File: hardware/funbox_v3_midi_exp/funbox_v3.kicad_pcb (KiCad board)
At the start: 2 copper layers, 59.7 x 67.5 mm, 70 parts, among them J6 MIDI IN JACK, J7 EXPRESSION, SW1 SW_SPDT, SW2 SW_SPDT, SW3 SW_SPDT, U1 TL074, U2 L7805, U3 TL072, U5 H11L1

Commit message: Updated to version 3.1, fix expression, adjusted pieces
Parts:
- J6: value MIDI IN JACK -> MIDI IN
- U3: value TL072 -> MCP6002
- moved R5 10.7 mm to (154.0, 129.9)
- moved R30 7.37 mm to (132.1, 66.4), turned to 0 degrees
- moved C30 6.62 mm to (133.4, 68.9), turned to -90 degrees
- moved R1 5.49 mm to (143.9, 129.9)
- moved C3 3.08 mm to (146.7, 126.8)
- moved C9 3.05 mm to (139.0, 126.9)
- moved R2 3.03 mm to (133.8, 129.9)
- moved S1 1.51 mm to (123.8, 117.0)
- moved J7 1.34 mm to (176.3, 71.2)
- moved J6 1.32 mm to (119.6, 71.2)
- moved 9v 0.83 mm to (144.2, 66.0)
- moved Gnd 0.80 mm to (148.2, 66.0)
- moved R19 0.73 mm to (162.9, 66.4)
- moved D2 0.67 mm to (136.2, 69.0)
- moved R31 0.59 mm to (138.9, 69.0)
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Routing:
- net Net-(U1A-+): track 27.0 -> 19.7 mm
- net DIP2: track 30.8 -> 25.1 mm
- net FOOT_SWITCH_2: track 74.9 -> 70.5 mm
- net Net-(D2-K): track 12.5 -> 8.27 mm
- net MIDI_IN_JACK_PIN4: track 9.64 -> 7.29 mm
- net MIDI_IN_JACK_PIN5: track 19.9 -> 17.7 mm
- net Net-(U1B-+): track 59.2 -> 61.2 mm
- net DIP1: track 23.9 -> 25.4 mm
- net EXPRESSION_REF: track 21.6 -> 20.3 mm
- net VCC: track 62.9 -> 64.1 mm
- net DIP4: track 41.2 -> 40.1 mm
- net DIP3: track 39.9 -> 38.8 mm
- net 3V3_A: track 153.9 -> 154.9 mm
- net EXPRESSION_IN_JACK: track 12.0 -> 11.0 mm
- net MIDI_IN: track 26.8 -> 27.6 mm
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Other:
- board text added: "FunBox v3.1 GuitarML"
- board text removed: "FunBox v3 GuitarML"

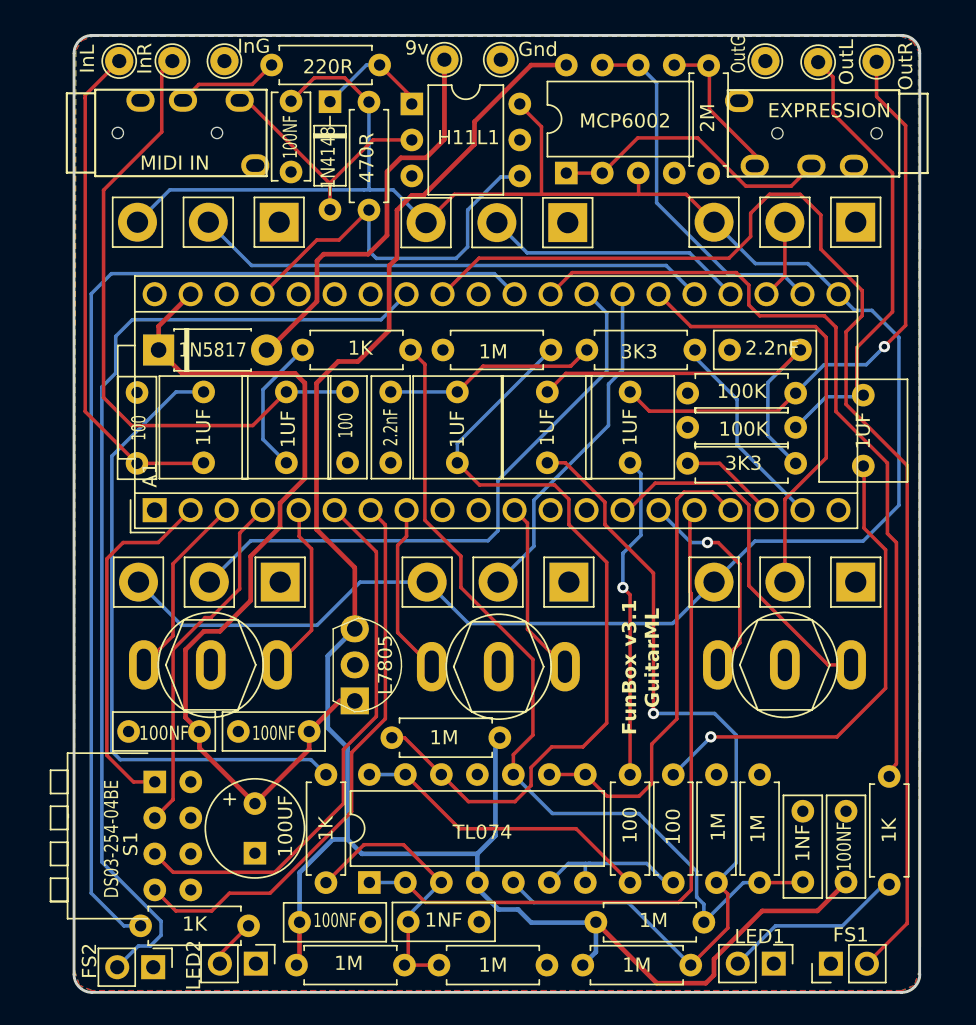
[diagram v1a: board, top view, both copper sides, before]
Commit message: Added pF label for clarity
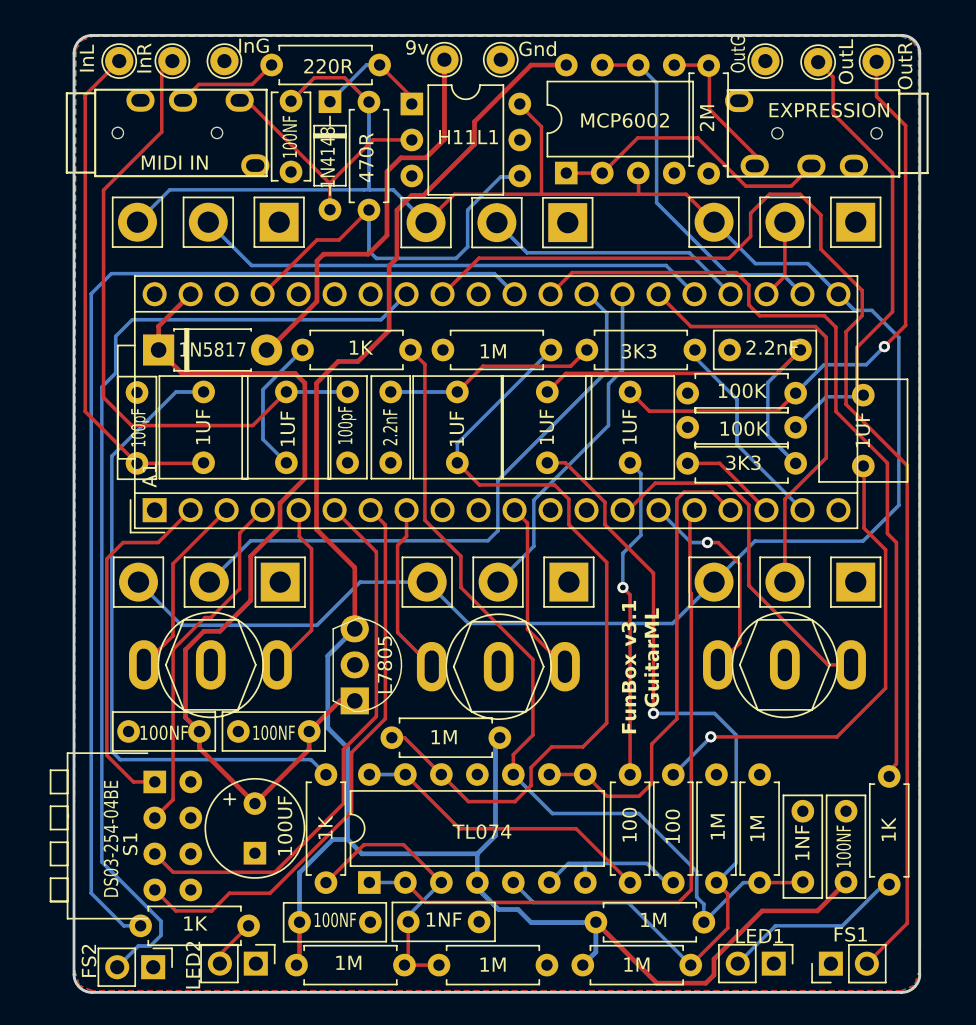
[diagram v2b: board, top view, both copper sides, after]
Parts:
- C11, C2: value 100 -> 100pF
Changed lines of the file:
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@@
         (effects (font (size 1 1) (thickness 0.15)))
     )
-    (fp_text value "100" (at 2.373 0.127 90) (layer "F.SilkS")
-        (effects (font (size 1 0.6952) (thickness 0.15)))
+    (fp_text value "100pF" (at 2.373 0.127 90) (layer "F.SilkS")
+        (effects (font (size 1 0.652) (thickness 0.15)))
     )
     (fp_text user "${REFERENCE}" (at 2.5 0 90) (layer "F.Fab")
@@
     )
     (fp_text value "100NF" (at 2.5 0.127 90) (layer "F.SilkS")
-        (effects (font (size 1 0.7968) (thickness 0.15)))
+        (effects (font (size 1 0.7) (thickness 0.15)))
     )
     (fp_text user "${REFERENCE}" (at 2.5 0 90) (layer "F.Fab")
@@
         (effects (font (size 1 1) (thickness 0.15)))
     )
-    (fp_text value "100" (at 2.5 0.127 90) (layer "F.SilkS")
-        (effects (font (size 1 0.6952) (thickness 0.15)))
+    (fp_text value "100pF" (at 2.5 0.127 90) (layer "F.SilkS")
+        (effects (font (size 1 0.652) (thickness 0.15)))
     )
     (fp_text user "${REFERENCE}" (at 2.5 0 90) (layer "F.Fab")

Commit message: Updated board to v3.2 to use MCP6024 op amp instead of TL074
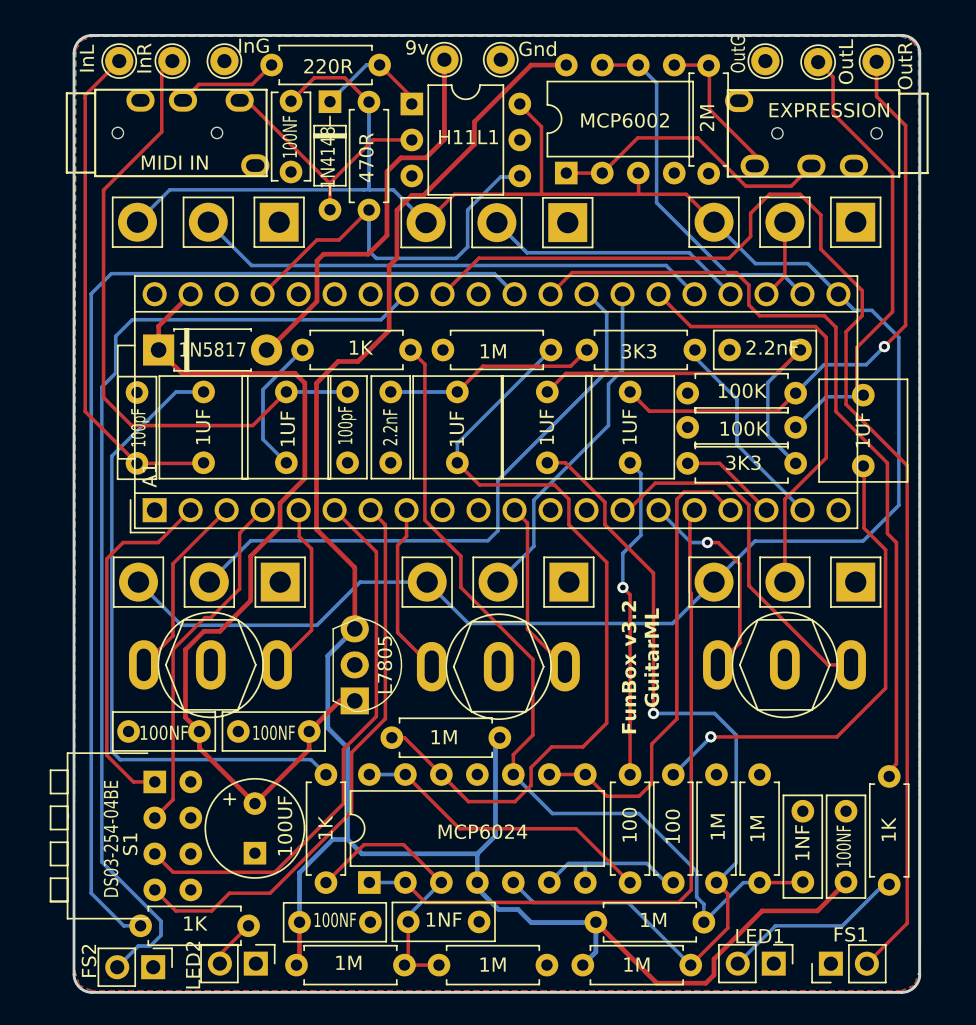
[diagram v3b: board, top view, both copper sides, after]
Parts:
- U1: value TL074 -> MCP6024
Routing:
- net GND: track 1.72 -> 0.00 mm
- net 5V: track 135.6 -> 134.9 mm
- net LED_1: track 57.7 -> 57.0 mm
- net unconnected-(A1-I2C1_SCL-Pad12): track 0.51 -> 0.00 mm
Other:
- board text added: "FunBox v3.2 GuitarML"
- board text removed: "FunBox v3.1 GuitarML"
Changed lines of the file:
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@@
       (plotinvisibletext false)
       (sketchpadsonfab false)
-      (subtractmaskfromsilk false)
+      (subtractmaskfromsilk true)
       (outputformat 1)
       (mirror false)
       (drillshape 0)
       (scaleselection 1)
-      (outputdirectory "GerberSeed/")
+      (outputdirectory "GerberSeed_PCBway_Funbox_v3p2/")
     )
   )
@@
         (effects (font (size 1 1) (thickness 0.15)))
     )
-    (fp_text value "TL074" (at 3.546 7.986 180) (layer "F.SilkS")
+    (fp_text value "MCP6024" (at 3.546 7.986 180) (layer "F.SilkS")
         (effects (font (size 1 1) (thickness 0.15)))
     )
@@
   (gr_line (start 118.11 130.556) (end 118.11 65.5574)
     (stroke (width 0.2) (type default)) (layer "Edge.Cuts"))
-  (gr_text "FunBox v3.1\n    GuitarML" (at 159.512 113.665 90) (layer "F.SilkS")
+  (gr_text "FunBox v3.2\n    GuitarML" (at 159.512 113.665 90) (layer "F.SilkS")
     (effects (font (size 1 1) (thickness 0.2) bold) (justify left bottom))
   )
@@
   (segment (start 139.7796 84.35) (end 122.225 84.35) (width 0.25) (layer "B.Cu") (net 5))
   (segment (start 121.05 88.119) (end 120.075 89.094) (width 0.25) (layer "B.Cu") (net 5))
-  (segment (start 121.478991 130.048) (end 121.158 130.048) (width 0.25) (layer "B.Cu") (net 5))
   (segment (start 123.5 128.55) (end 122.656 128.55) (width 0.25) (layer "B.Cu") (net 5))
   (segment (start 122.225 84.35) (end 121.05 85.525) (width 0.25) (layer "B.Cu") (net 5))
@@
   (segment (start 134 99.65) (end 134 97.8304) (width 0.25) (layer "F.Cu") (net 7))
   (segment (start 134.875 100.525) (end 134 99.65) (width 0.25) (layer "F.Cu") (net 7))
-  (segment (start 133.704004 97.79) (end 133.9596 97.79) (width 0.25) (layer "F.Cu") (net 7))
   (segment (start 132.4356 108.712) (end 134.875 106.2726) (width 0.25) (layer "F.Cu") (net 7))
   (segment (start 134 97.8304) (end 133.9596 97.79) (width 0.25) (layer "F.Cu") (net 7))
@@
   (segment (start 140.95 106.4314) (end 140.95 100.271301) (width 0.25) (layer "F.Cu") (net 9))
   (segment (start 141.5796 99.641701) (end 141.5796 97.79) (width 0.25) (layer "F.Cu") (net 9))
-  (segment (start 152.2476 97.79) (end 151.7396 97.79) (width 0.25) (layer "F.Cu") (net 10))
   (segment (start 161.671 103.666364) (end 161.671 124.587) (width 0.25) (layer "F.Cu") (net 14))
   (segment (start 161.5788 98.1108) (end 161.5788 103.574164) (width 0.25) (layer "F.Cu") (net 14))
@@
   (segment (start 163.6776 94.488) (end 166.9796 97.79) (width 0.25) (layer "F.Cu") (net 15))
   (segment (start 161.417 94.488) (end 163.6776 94.488) (width 0.25) (layer "F.Cu") (net 15))
-  (segment (start 167.259 97.5106) (end 166.9796 97.79) (width 0.25) (layer "B.Cu") (net 15))
-  (segment (start 127.635 108.1786) (end 127.635 108.9152) (width 0.25) (layer "F.Cu") (net 16))
-  (segment (start 146.685 116.337) (end 146.573 116.449) (width 0.25) (layer "F.Cu") (net 16))
-  (segment (start 173.860999 102.287801) (end 173.2788 102.87) (width 0.25) (layer "F.Cu") (net 16))
   (segment (start 168.2788 77.47) (end 168.2788 81.2762) (width 0.25) (layer "F.Cu") (net 17))
   (segment (start 168.2788 81.2762) (end 167.005 82.55) (width 0.25) (layer "F.Cu") (net 17))
@@
   (segment (start 159.3596 82.55) (end 161.6456 84.836) (width 0.25) (layer "F.Cu") (net 20))
   (segment (start 170.434 84.836) (end 171.196 85.598) (width 0.25) (layer "F.Cu") (net 20))
-  (segment (start 159.385 82.55) (end 159.705991 82.55) (width 0.25) (layer "B.Cu") (net 20))
   (segment (start 160.655 97.028) (end 161.163 96.52) (width 0.25) (layer "F.Cu") (net 21))
   (segment (start 160.655 112.522) (end 160.655 97.028) (width 0.25) (layer "F.Cu") (net 21))
@@
   (segment (start 164.846 81.026) (end 153.2636 81.026) (width 0.25) (layer "F.Cu") (net 23))
   (segment (start 171.8818 84.8868) (end 171.069 84.074) (width 0.25) (layer "F.Cu") (net 23))
-  (segment (start 152.4 82.55) (end 151.765 82.55) (width 0.25) (layer "B.Cu") (net 23))
   (segment (start 119.325 82.525) (end 119.325 124.825) (width 0.25) (layer "B.Cu") (net 24))
   (segment (start 119.325 124.825) (end 121.627 127.127) (width 0.25) (layer "B.Cu") (net 24))
@@
   (segment (start 145.075 80.025) (end 139.45 80.025) (width 0.25) (layer "B.Cu") (net 30))
   (segment (start 139.45 80.025) (end 138.925 79.5) (width 0.25) (layer "B.Cu") (net 30))
-  (segment (start 120.5992 66.167) (end 120.5992 66.2008) (width 0.25) (layer "F.Cu") (net 31))
   (segment (start 122.555 94.488) (end 127.214 94.488) (width 0.25) (layer "F.Cu") (net 31))
   (segment (start 127.214 94.488) (end 127.254 94.448) (width 0.25) (layer "F.Cu") (net 31))
@@
   (segment (start 118.9 68.7) (end 118.9 68.5) (width 0.25) (layer "F.Cu") (net 31))
   (segment (start 118.8974 90.8304) (end 118.8974 68.7026) (width 0.25) (layer "F.Cu") (net 31))
-  (segment (start 123.19 94.361) (end 123.19 94.448) (width 0.25) (layer "F.Cu") (net 31))
-  (segment (start 135.89 116.586) (end 135.89 116.332) (width 0.25) (layer "F.Cu") (net 32))
   (segment (start 120.777 114.808) (end 121.369 115.4) (width 0.25) (layer "B.Cu") (net 32))
   (segment (start 120.777 93.98) (end 120.777 114.808) (width 0.25) (layer "B.Cu") (net 32))
@@
   (segment (start 171.675 67.225) (end 171.675 69.8) (width 0.25) (layer "F.Cu") (net 35))
   (segment (start 170.625 66.175) (end 171.675 67.225) (width 0.25) (layer "F.Cu") (net 35))
-  (segment (start 170.0276 66.3194) (end 170.0276 66.4276) (width 0.25) (layer "F.Cu") (net 35))
   (segment (start 175.875 74) (end 175.875 83.8) (width 0.25) (layer "F.Cu") (net 35))
   (segment (start 171.675 69.8) (end 175.875 74) (width 0.25) (layer "F.Cu") (net 35))
@@
   (segment (start 150.114 106.1974) (end 150.114 98.7044) (width 0.25) (layer "F.Cu") (net 41))
   (segment (start 125.975 112.426) (end 126.96 113.411) (width 0.3302) (layer "F.Cu") (net 43))
-  (segment (start 134.707 113.411) (end 134.473 113.411) (width 0.3302) (layer "F.Cu") (net 43))
   (segment (start 134.4 88.825) (end 134.4 95.55) (width 0.3302) (layer "F.Cu") (net 43))
-  (segment (start 126.3396 82.55) (end 126.3396 82.7786) (width 0.25) (layer "F.Cu") (net 43))
   (segment (start 134.707 113.411) (end 134.707 114.668) (width 0.3302) (layer "F.Cu") (net 43))
   (segment (start 126.96 114.585) (end 130.875 118.5) (width 0.3302) (layer "F.Cu") (net 43))
@@
   (segment (start 142.775 75.575) (end 146.375 71.975) (width 0.3302) (layer "F.Cu") (net 44))
   (segment (start 140.35 80.55) (end 140.9 80) (width 0.3302) (layer "F.Cu") (net 44))
-  (segment (start 138.049 106.553) (end 137.8646 106.3686) (width 0.25) (layer "F.Cu") (net 44))
   (segment (start 163.275 130.6) (end 162.7 131.175) (width 0.3302) (layer "F.Cu") (net 44))
   (segment (start 166.675 126.075) (end 163.275 129.475) (width 0.3302) (layer "F.Cu") (net 44))
   (segment (start 172.593 124.057) (end 170.575 126.075) (width 0.3302) (layer "F.Cu") (net 44))
-  (segment (start 152.58 66.675) (end 152.875 66.38) (width 0.3302) (layer "F.Cu") (net 44))
   (segment (start 146.375 70.375) (end 150.37 66.38) (width 0.3302) (layer "F.Cu") (net 44))
   (segment (start 140.9 76.625) (end 141.95 75.575) (width 0.3302) (layer "F.Cu") (net 44))
@@
   (segment (start 166.497 124.079) (end 169.505 124.079) (width 0.25) (layer "F.Cu") (net 54))
   (segment (start 142.875 98.50655) (end 145.415 101.04655) (width 0.25) (layer "F.Cu") (net 54))
-  (segment (start 168.997 124.079) (end 169.037 124.039) (width 0.25) (layer "F.Cu") (net 54))
-  (segment (start 169.505 124.079) (end 169.545 124.039) (width 0.25) (layer "F.Cu") (net 54))
   (segment (start 145.415 101.04655) (end 145.415 103.251) (width 0.25) (layer "F.Cu") (net 54))
   (segment (start 142.875 87.503) (end 142.875 98.50655) (width 0.25) (layer "F.Cu") (net 54))
